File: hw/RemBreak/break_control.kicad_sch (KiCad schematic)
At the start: 13 parts, among them J6 Conn_01x07, J7 Conn_01x07, J8 Conn_01x03, Q10 BC337, Q11 BC847

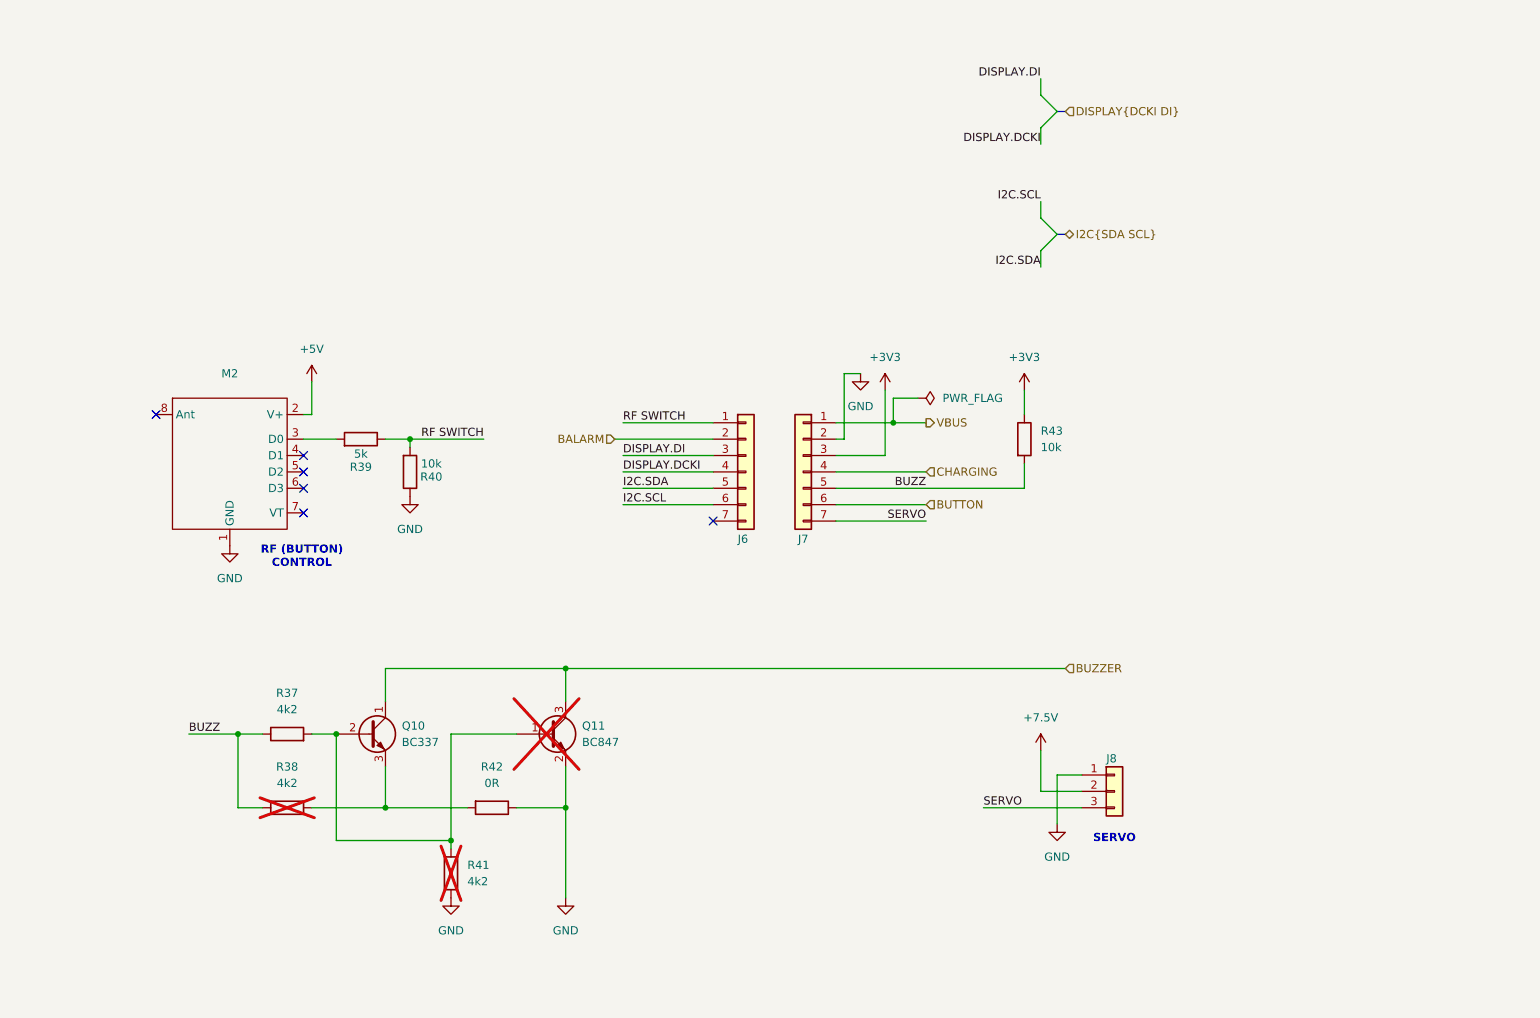
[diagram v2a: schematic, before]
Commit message: redrawing the schematics according the notes from the module design
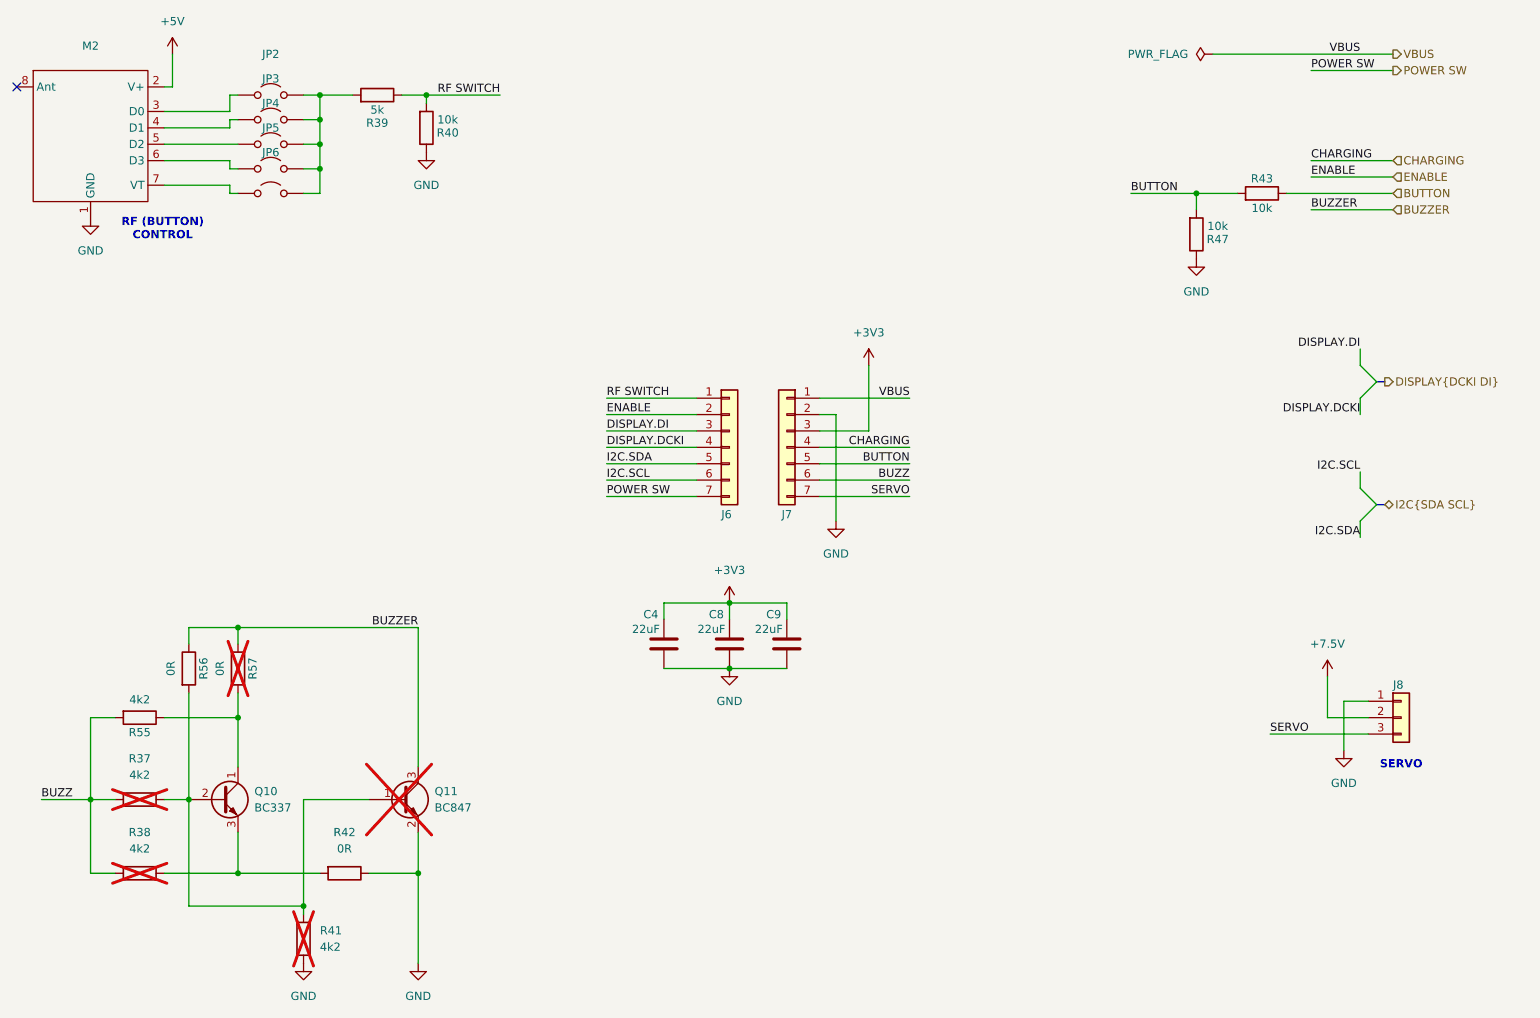
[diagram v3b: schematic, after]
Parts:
- added C4, C8, C9: 22uF, Capacitor_SMD:C_0805_2012Metric_Pad1.18x1.45mm_HandSolder, symbol Device:C
- added JP2, JP3, JP4, JP5, JP6: Jumper_2_Open, symbol Jumper:Jumper_2_Open
- added R47: 10k, Resistor_SMD:R_0805_2012Metric_Pad1.20x1.40mm_HandSolder, symbol Device:R
- added R55: 4k2, Resistor_SMD:R_0805_2012Metric_Pad1.20x1.40mm_HandSolder, symbol Device:R
- added R56, R57: 0R, Resistor_SMD:R_0805_2012Metric_Pad1.20x1.40mm_HandSolder, symbol Device:R
- R37: now not fitted
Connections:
- net +3V3: now also C4.1, C8.1, C9.1; no longer R43.1
- net BUTTON: now also J7.5 (Pin_5), R43.1, R43.2, R47.2; no longer J7.6 (Pin_6)
- net BUZZ: now also J7.6 (Pin_6), R55.2; no longer J7.5 (Pin_5), R43.2
- net BUZZER: now also R56.1, R57.1; no longer Q10.1 (C)
- net GND: now also C4.2, C8.2, C9.2, R47.1
- net at Q10.2 (B), Q11.1 (B), R37.2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: now also R56.2
- net POWER SW: now reaches J6.7 (Pin_7)
- net at R39.2: now also JP2.2 (B), JP3.2 (B), JP4.2 (B), JP5.2 (B), JP6.2 (B); no longer M2.3 (D0)
- net at M2.4 (D1): now also JP3.1 (A)
- net at M2.5 (D2): now also JP4.1 (A)
- net at M2.6 (D3): now also JP5.1 (A)
- net at M2.7 (VT): now also JP6.1 (A)
- net BALARM renamed ENABLE
- new net: Q10.1 (C), R55.1, R57.2
- new net: JP2.1 (A), M2.3 (D0)
- no-connect marks 6 -> 1
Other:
- moved on the sheet: J6, J7, J8, M2, Q10, Q11, R38, R39, R40, R41, R42
